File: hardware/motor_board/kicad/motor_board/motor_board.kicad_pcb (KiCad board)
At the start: 4 copper layers, 75 x 35 mm, 237 parts, among them J1 BOOMELE_1.27-2x10P, J2 WAFER-SH1.0-6PWB, J3 WAFER-SH1.0-6PWB, J4 S5B-XH-A, Q1 HYG015N04LS1C2, Q2 HYG015N04LS1C2, Q3 HYG015N04LS1C2, Q4 HYG015N04LS1C2, Q5 HYG015N04LS1C2, Q6 HYG015N04LS1C2, Q7 HYG015N04LS1C2, Q8 HYG015N04LS1C2, U1 STM32G474RET6, U10 SN74LVC3G17DCUR, U11 TPS22945DCKR, U12 TPS22945DCKR, U13 LM74502DDFR, U14 74LVC1G17SE-7, U2 DRV8323RHRGZR, U3 DRV8316CRRGFR, U4 DRV8316CRRGFR, U5 AP2112K-3.3TRG1, U6 SN74LVC08APWR, U7 INA239AIDGSR, U8 BQ76907RGRR, U9 SN74LVC3G17DCUR

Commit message: motor_board routing block 2: U2 local (buck loop, charge pump lanes, straps, FB/EN dividers), DRC 0
Charge-pump caps C20/C21 swapped (C20 flipped) so pins 5/4/3 fan out without crossing;
R20/R21 0.1 mm rearward for courtyard room.

Co-Authored-By: Claude Opus 5.5 (1M context) <noreply@anthropic.com>
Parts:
- moved C20 2.95 mm to (159.4, 95.3), turned to 180 degrees
- moved C21 2.69 mm to (160.4, 92.5), turned to 90 degrees
- moved R20 0.10 mm to (158.7, 96.6)
- moved R21 0.10 mm to (160.7, 96.6)
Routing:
- net /weapon/BUCK_EN: track 0.00 -> 18.8 mm, vias 0 -> 2
- net /weapon/BUCK_SW: track 0.00 -> 11.0 mm
- net VBAT: track 0.00 -> 10.5 mm
- net /weapon/U2_VDS: track 0.00 -> 4.37 mm
- net /weapon/BUCK_FB: track 0.00 -> 4.10 mm
- net /weapon/U2_VCP: track 0.00 -> 3.95 mm
- net /weapon/U2_CPH: track 0.00 -> 3.62 mm
- net /weapon/BUCK_CB: track 0.00 -> 3.13 mm
- net /weapon/U2_IDRIVE: track 0.00 -> 1.56 mm
- net /weapon/U2_CPL: track 0.00 -> 1.40 mm
- net /weapon/U2_DVDD: track 0.00 -> 1.28 mm
- net +3V3: track 0.00 -> 1.28 mm
- net /weapon/U2_MODE: track 0.00 -> 1.25 mm

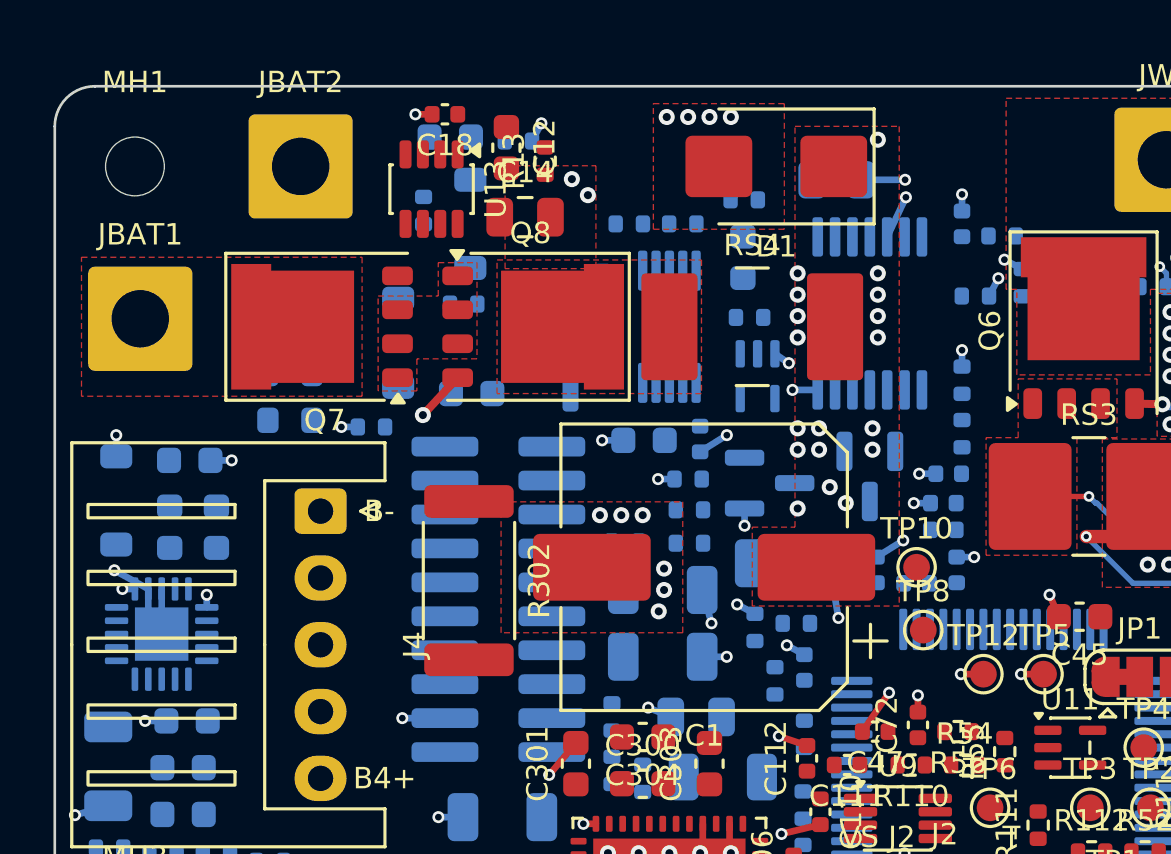
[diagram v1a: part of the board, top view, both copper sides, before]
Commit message: motor_board routing block 3: power-switch corner (auto pairs, 71 of 84; 13 left for hand routing), DRC 0
make_pairs.py freezes a block's connection list from DRC; router gets a retry pass.
Survey of the rest (not kept) shows the greedy router's limit in the logic areas.

Co-Authored-By: Claude Opus 5.5 (1M context) <noreply@anthropic.com>
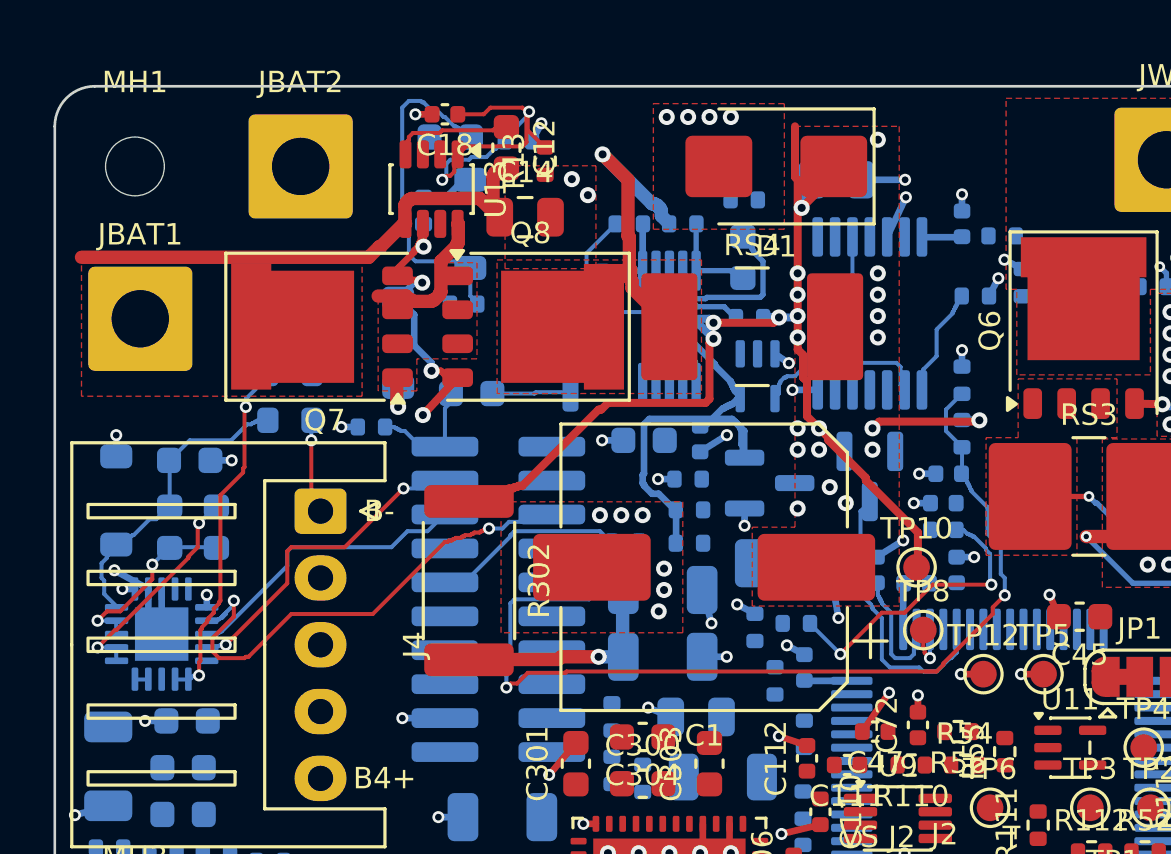
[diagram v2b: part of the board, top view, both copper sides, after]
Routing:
- net VBAT: track 10.5 -> 60.7 mm, vias 49 -> 54
- net /mcu/VBAT_SNS: track 0.00 -> 38.5 mm, vias 0 -> 2
- net +3V3: track 1.28 -> 30.9 mm
- net /power/BAT_IN: track 0.00 -> 19.6 mm
- net BMS_SCL: track 0.00 -> 18.8 mm, vias 0 -> 2
- net /power/PSW_EN: track 0.00 -> 14.2 mm, vias 0 -> 2
- net W_ARM_S: track 0.00 -> 13.9 mm
- net /power/BMS_BAT: track 0.00 -> 13.3 mm, vias 0 -> 2
- net /power/PSW_DV: track 0.00 -> 12.8 mm
- net BMS_ALERT: track 0.00 -> 12.2 mm, vias 0 -> 2
- net /power/CELL0: track 0.00 -> 11.4 mm
- net /power/VBAT_SW: track 0.00 -> 11.2 mm, vias 0 -> 1
- net /mcu/L_SOC_F: track 0.00 -> 11.2 mm, vias 0 -> 2
- net BMS_SDA: track 0.00 -> 11.1 mm
- net /power/PSW_G: track 1.91 -> 12.5 mm, vias 1 -> 4
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
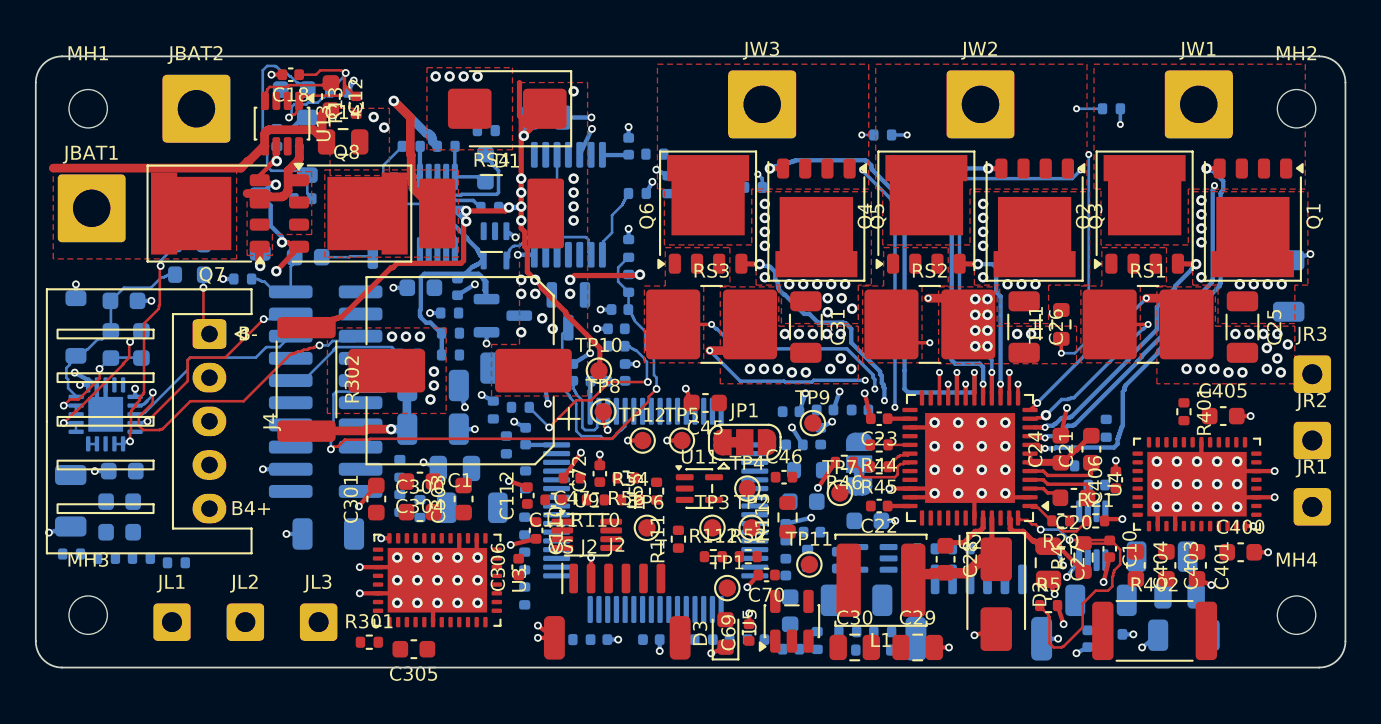
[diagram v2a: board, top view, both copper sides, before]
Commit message: motor_board routing: ROUTING_PLAN.md; U1 fan-out under its body (39 pins); test pads moved off U1's footprint; GND drop-via block; geo.py clearance helper
Co-Authored-By: Claude Opus 5.5 (1M context) <noreply@anthropic.com>
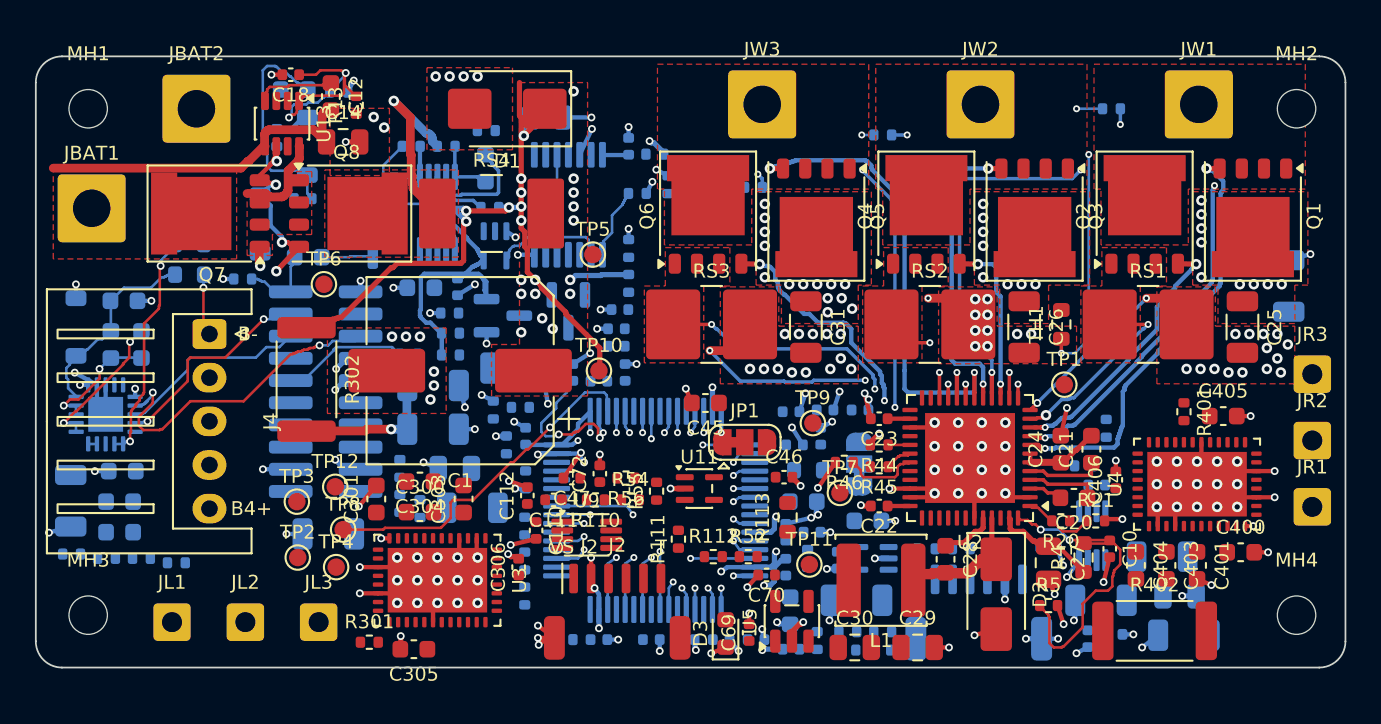
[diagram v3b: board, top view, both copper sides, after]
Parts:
- moved TP2 26.1 mm to (115.0, 98.7)
- moved TP4 24.0 mm to (117.2, 99.2)
- moved TP3 23.8 mm to (115.0, 95.5)
- moved TP6 23.2 mm to (116.5, 83.0)
- moved TP1 22.5 mm to (158.9, 88.8)
- moved TP12 17.8 mm to (117.2, 94.7)
- moved TP8 16.4 mm to (117.6, 97.1)
- moved TP5 11.8 mm to (131.9, 81.3)
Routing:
- net GND: track 96.5 -> 138.1 mm, vias 178 -> 216
- net /mcu/VBAT_SNS: track 38.5 -> 2.98 mm, vias 2 -> 1
- net DRV_OFF: track 2.23 -> 19.9 mm
- net /mcu/L_SOC_F: track 11.2 -> 1.22 mm, vias 2 -> 1
- net L_MTEMP: track 10.5 -> 1.31 mm, vias 0 -> 1
- net +3V3: track 30.9 -> 37.1 mm, vias 0 -> 4
- net W_nFAULT: track 4.84 -> 10.9 mm, vias 0 -> 3
- net R_nCS: track 0.00 -> 4.64 mm, vias 0 -> 1
- net R_S3: track 0.00 -> 3.68 mm, vias 0 -> 1
- net R_INHC: track 0.00 -> 3.33 mm, vias 0 -> 1
- net W_INHC: track 0.00 -> 3.24 mm, vias 0 -> 1
- net W_EN: track 0.00 -> 3.24 mm, vias 0 -> 1
- net /mcu/L_SOA_F: track 0.00 -> 3.24 mm, vias 0 -> 1
- net /mcu/+3V3A: track 0.00 -> 2.97 mm, vias 0 -> 2
- net R_S2: track 0.00 -> 1.93 mm, vias 0 -> 1
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
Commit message: motor_board routing blocks 6a/6: U3/U4 charge pump + VM caps re-placed to pin order (U4 mirrors U3, C400 on the bottom), AVDD/FBBK/SWBK hookups; TP8/TP12 moved again
Co-Authored-By: Claude Opus 5.5 (1M context) <noreply@anthropic.com>
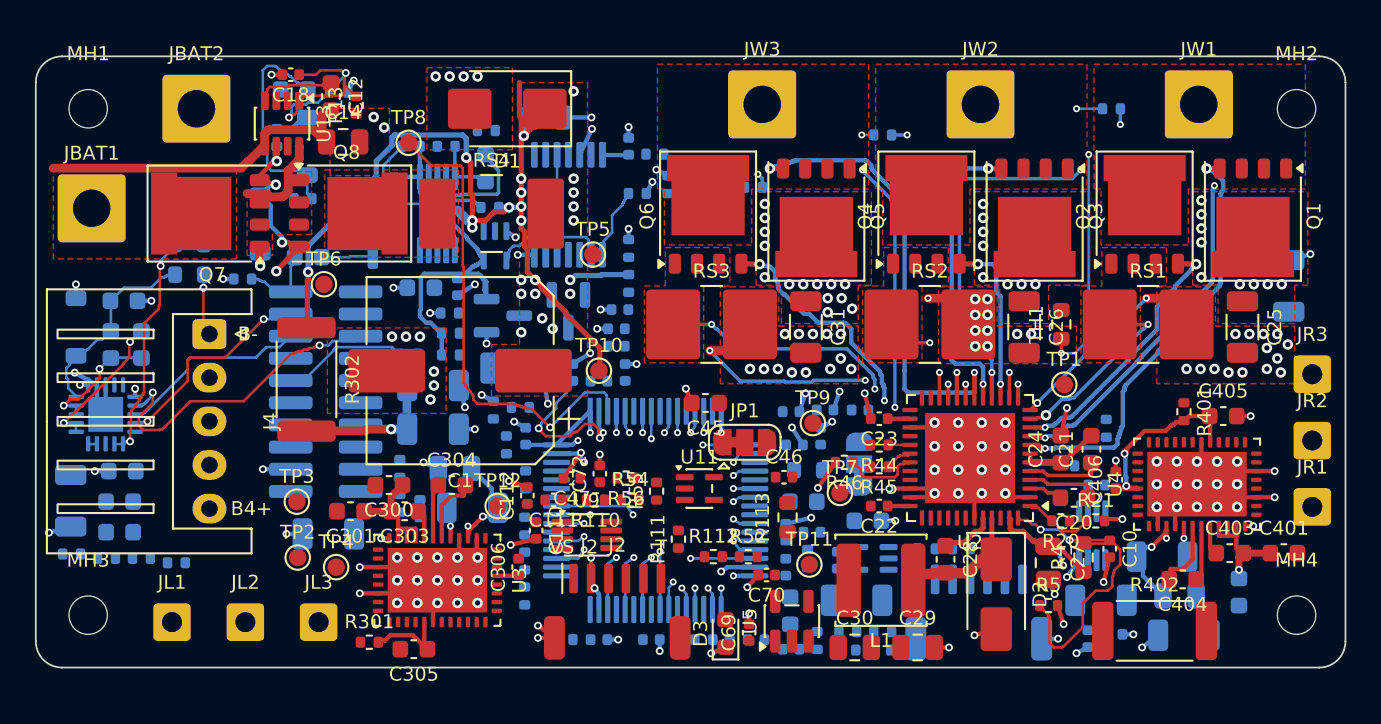
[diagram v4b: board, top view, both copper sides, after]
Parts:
- C400: moved to B.Cu
- moved TP8 22.5 mm to (121.3, 75.0)
- moved TP12 9.36 mm to (126.5, 95.8)
- moved C401 5.02 mm to (171.5, 98.5), turned to 0 degrees
- moved C403 3.69 mm to (168.4, 98.5), turned to 0 degrees
- moved C303 3.45 mm to (121.1, 96.0), turned to 180 degrees
- moved C404 2.79 mm to (165.7, 100.0), turned to 180 degrees
- moved C300 2.36 mm to (120.2, 94.5), turned to 180 degrees
- moved C400 2.28 mm to (168.9, 100.7), turned to -90 degrees
- moved C304 1.84 mm to (123.8, 94.5), turned to 0 degrees
- moved C301 1.63 mm to (118.0, 96.0), turned to 180 degrees
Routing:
- net GND: track 138.1 -> 96.7 mm, vias 216 -> 176
- net /drive_right/R_AVDD: track 0.00 -> 11.2 mm, vias 0 -> 2
- net /power/VBAT_SW: track 11.2 -> 0.00 mm, vias 1 -> 0
- net VBAT: track 59.4 -> 70.0 mm, vias 53 -> 55
- net DRV_OFF: track 19.9 -> 27.3 mm
- net /drive_left/L_AVDD: track 0.00 -> 6.18 mm
- net /drive_left/L_VM: track 8.33 -> 14.3 mm
- net /drive_right/R_VM: track 0.00 -> 5.75 mm, vias 0 -> 1
- net /drive_left/L_FBBK: track 0.00 -> 5.74 mm, vias 0 -> 2
- net /drive_right/R_FBBK: track 0.00 -> 5.71 mm, vias 0 -> 2
- net /drive_left/L_CPL: track 0.00 -> 3.49 mm
- net /drive_right/R_CPL: track 0.00 -> 3.49 mm
- net /drive_right/R_CPH: track 0.00 -> 2.55 mm
- net /drive_left/L_CPH: track 0.00 -> 2.55 mm
- net /drive_right/R_CP: track 0.00 -> 1.05 mm
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
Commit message: motor_board routing block 6b: motor outputs (0.8 mm top lanes, pin order = connector order), U3/U4 GND pins 15/18 into the EP; TP2/TP4 over U1's front row
Co-Authored-By: Claude Opus 5.5 (1M context) <noreply@anthropic.com>
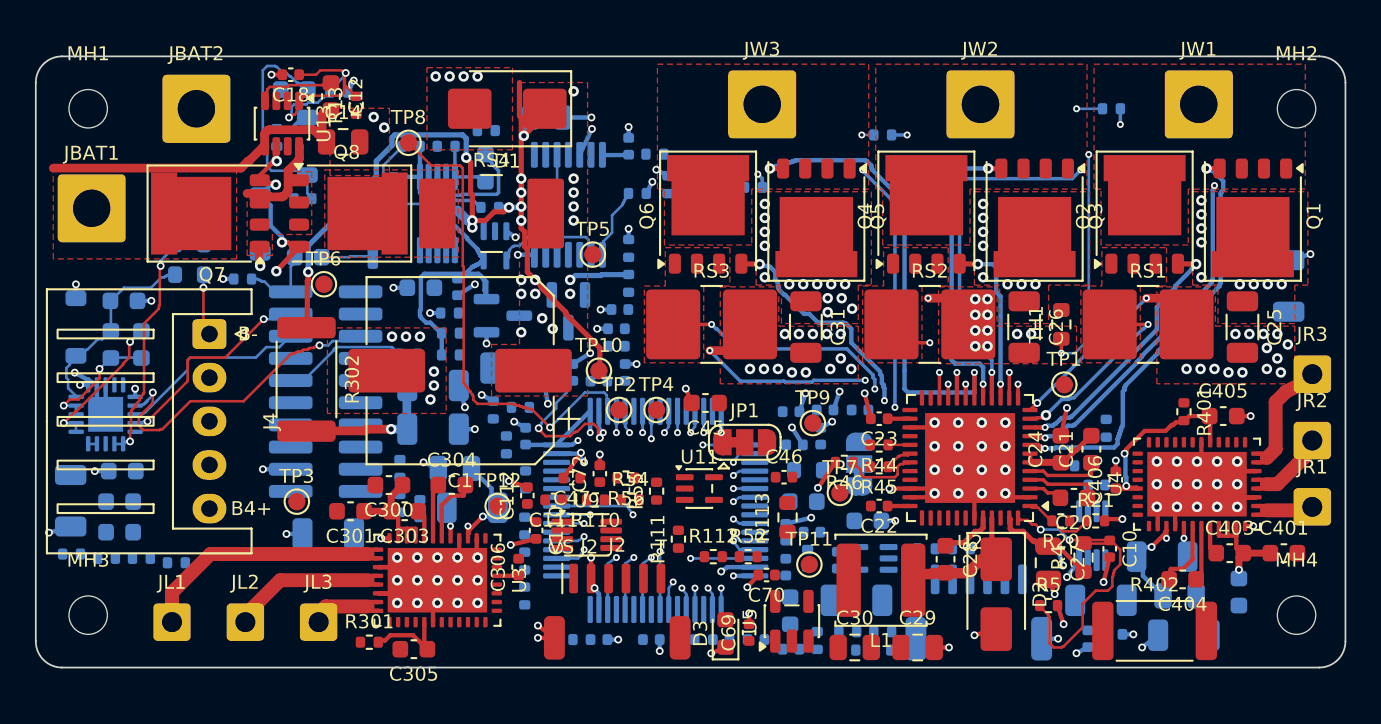
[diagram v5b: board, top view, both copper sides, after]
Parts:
- moved TP4 20.4 mm to (135.6, 90.2)
- moved TP2 20.2 mm to (133.4, 90.2)
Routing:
- net /drive_left/L_A: track 0.00 -> 15.5 mm
- net /drive_left/L_B: track 0.00 -> 9.93 mm
- net /drive_right/R_C: track 0.00 -> 7.07 mm
- net /drive_right/R_B: track 0.00 -> 5.13 mm
- net /drive_left/L_C: track 0.00 -> 4.67 mm
- net /drive_right/R_A: track 0.00 -> 4.30 mm
- net GND: track 96.7 -> 95.7 mm, vias 176 -> 172

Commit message: motor_board routing blocks 6c/6d: VM trunks (R302 -> U3 VM caps, R402 -> U4 VM caps) and bulk-cap links; pick_via/geo_why helpers (spots checked before DRC). C309/C310 (L) and C409 (R) bulk left for close-out (badly placed)
Co-Authored-By: Claude Opus 5.5 (1M context) <noreply@anthropic.com>
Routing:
- net /drive_right/R_VM: track 5.75 -> 29.5 mm, vias 1 -> 5
- net /drive_right/R_AVDD: track 11.2 -> 0.00 mm, vias 2 -> 0
- net /drive_left/L_VM: track 14.3 -> 21.8 mm, vias 1 -> 2
- net /drive_left/L_AVDD: track 6.18 -> 0.00 mm
- net /drive_left/L_FBBK: track 5.74 -> 0.45 mm, vias 2 -> 1
- net /drive_right/R_FBBK: track 5.71 -> 0.45 mm, vias 2 -> 1
